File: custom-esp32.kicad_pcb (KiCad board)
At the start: 2 copper layers, 26 parts, among them J3 USB_C_Receptacle_USB2.0_16P, U1 ESD7104MUTAG, U2 ENS210, U3 ESP32-S3-MINI-1-N8, U4 TLV75801PDRV

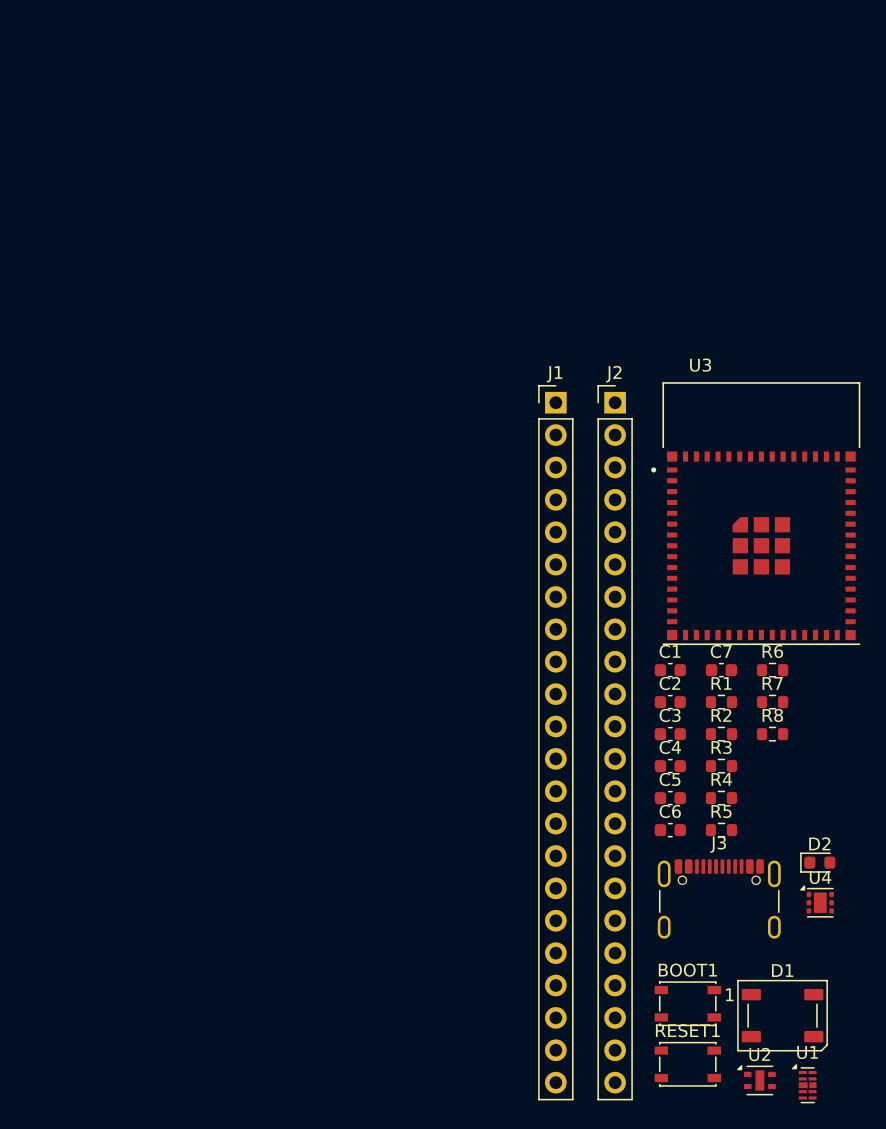
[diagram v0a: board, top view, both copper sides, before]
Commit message: Add initial pcb layout
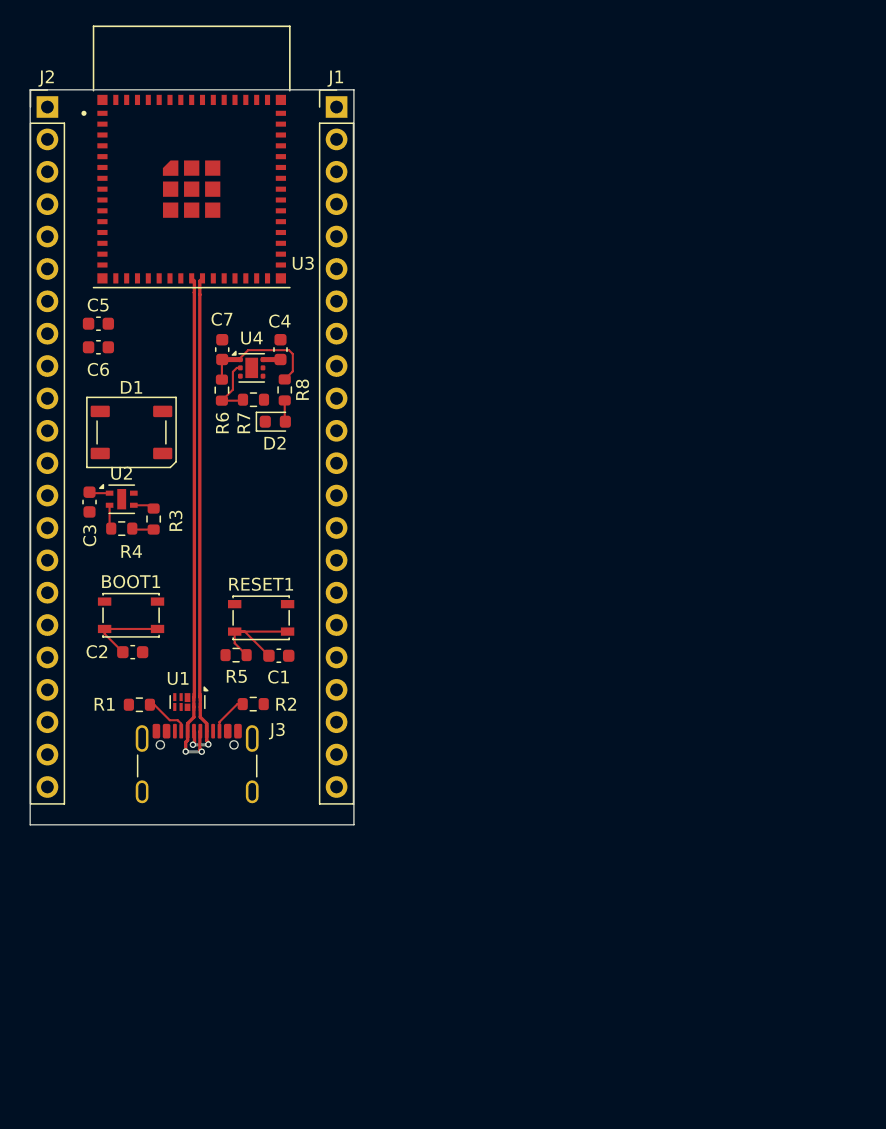
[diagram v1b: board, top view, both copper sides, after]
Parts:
- moved D1 68.6 mm to (97.5, 57.0)
- moved U2 67.7 mm to (96.7, 62.2)
- moved U4 61.2 mm to (106.9, 51.9)
- moved C6 58.7 mm to (94.9, 50.3)
- moved C5 58.3 mm to (94.9, 48.4)
- moved U1 57.2 mm to (101.9, 78.1), turned to -90 degrees
- moved D2 55.0 mm to (108.8, 56.1)
- moved BOOT1 53.3 mm to (97.5, 71.3)
- moved U3 52.7 mm to (102.2, 37.9)
- moved R4 51.6 mm to (96.7, 64.5)
- moved J2 50.2 mm to (90.9, 31.4)
- moved C3 49.1 mm to (94.2, 62.4), turned to -90 degrees
- moved R3 48.6 mm to (99.2, 63.8), turned to -90 degrees
- moved R6 48.5 mm to (104.6, 53.7), turned to 90 degrees
- moved RESET1 48.4 mm to (107.7, 71.5)
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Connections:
- U1 pad 10: unconnected-(U1-NC-Pad10) -> D+
- U1 pad 7: unconnected-(U1-NC-Pad7) -> 5VUSB
- U1 pad 9: unconnected-(U1-NC-Pad9) -> D-
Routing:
- net D-: track 0.00 -> 40.4 mm, vias 0 -> 2
- net D+: track 0.00 -> 39.3 mm, vias 0 -> 2
- net 3V3: track 0.00 -> 13.2 mm
- net ESP32_EN: track 0.00 -> 9.86 mm
- net GPIO0: track 0.00 -> 6.56 mm
- net Net-(U4-FB): track 0.00 -> 5.02 mm
- net Net-(J3-CC1): track 0.00 -> 3.66 mm
- net Net-(J3-CC2): track 0.00 -> 3.12 mm
- net I2C_SCL: track 0.00 -> 1.85 mm
- net Net-(D2-A): track 0.00 -> 1.69 mm
- net I2C_SDA: track 0.00 -> 1.66 mm
- net 5VUSB: track 0.00 -> 1.37 mm
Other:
- board outline added: 25.4 x 57.7 mm
- copper layers 2 -> 4

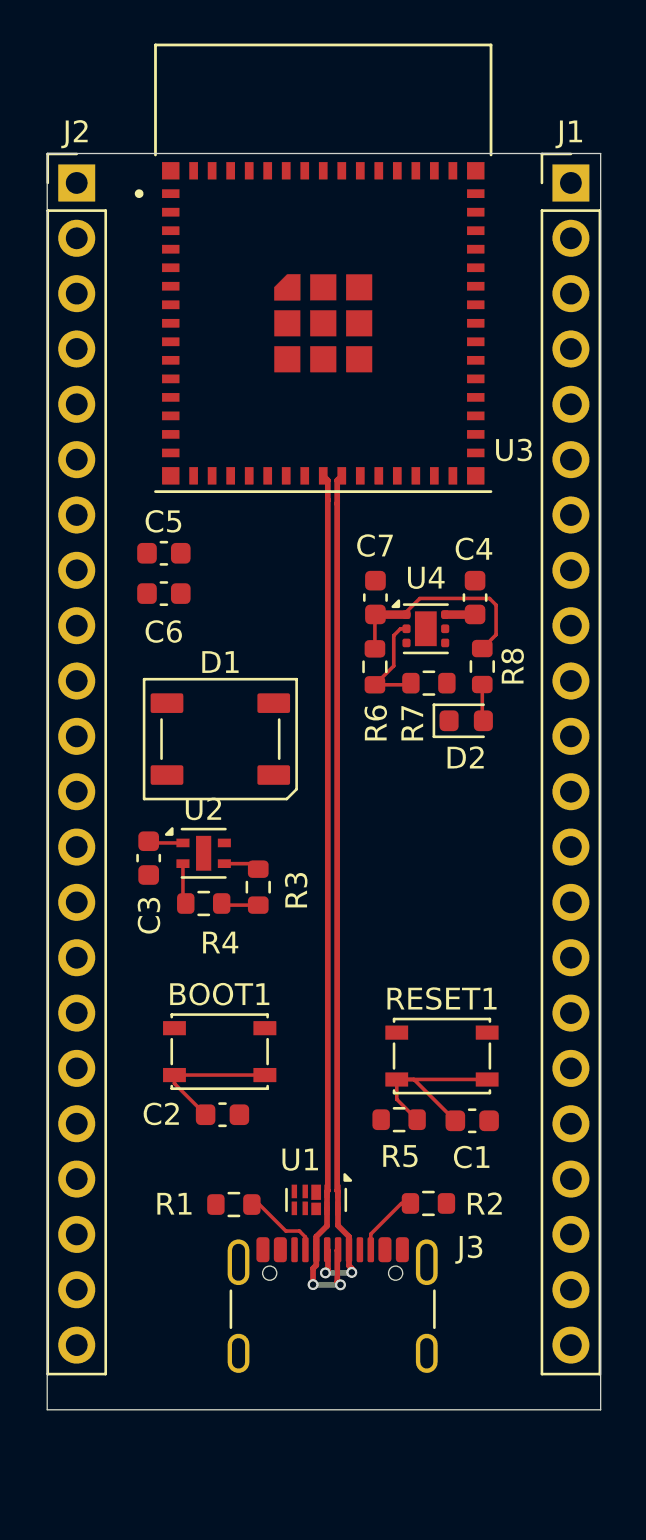
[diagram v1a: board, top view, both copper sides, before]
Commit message: Connect remaining components in pcb layout
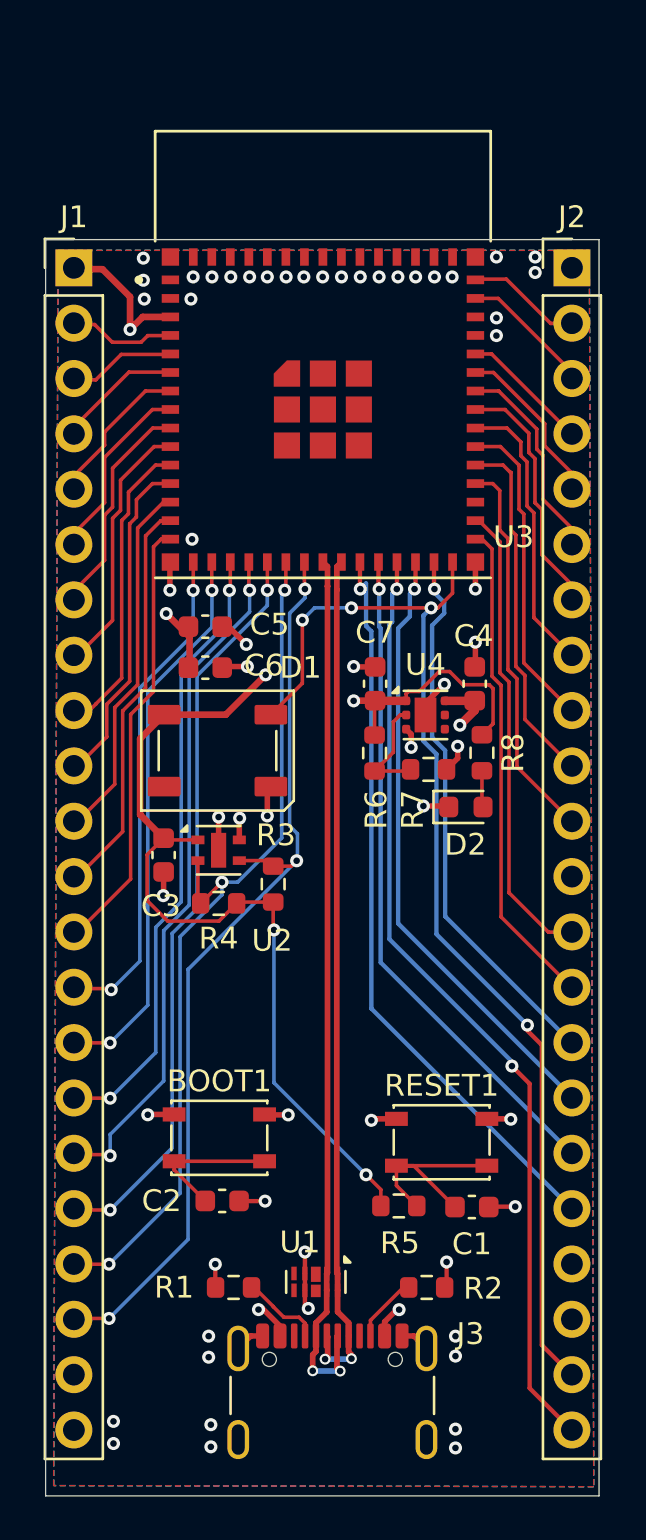
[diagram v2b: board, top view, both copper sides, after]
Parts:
- moved J1 23.1 mm to (90.8, 35.3)
- moved J2 23.1 mm to (113.6, 35.3)
- moved BOOT1 3.96 mm to (97.5, 75.3)
- moved C1 3.96 mm to (109.0, 78.4)
- moved C2 3.96 mm to (97.6, 78.2)
- moved R5 3.96 mm to (105.7, 78.4)
- moved RESET1 3.96 mm to (107.7, 75.5)
- moved C4 3.96 mm to (109.2, 54.4)
- moved C7 3.96 mm to (104.6, 54.4)
- moved D2 3.96 mm to (108.8, 60.1)
- moved R6 3.96 mm to (104.6, 57.6)
- moved R7 3.96 mm to (107.1, 58.4)
- moved R8 3.96 mm to (109.5, 57.6)
- moved U3 3.96 mm to (102.2, 41.8)
- moved U4 3.96 mm to (106.9, 55.9)
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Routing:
- net 3V3: track 13.2 -> 85.6 mm, vias 0 -> 6
- net GPIO48: track 0.00 -> 52.0 mm, vias 0 -> 4
- net 5VUSB: track 1.37 -> 52.0 mm, vias 0 -> 5
- net GPIO47: track 0.00 -> 43.5 mm, vias 0 -> 2
- net I2C_SDA: track 1.66 -> 43.1 mm, vias 0 -> 3
- net I2C_SCL: track 1.85 -> 40.8 mm, vias 0 -> 3
- net GPIO16: track 0.00 -> 34.3 mm, vias 0 -> 2
- net GPIO21: track 0.00 -> 34.2 mm, vias 0 -> 1
- net GPIO15: track 0.00 -> 31.5 mm, vias 0 -> 2
- net GPIO26: track 0.00 -> 30.8 mm, vias 0 -> 1
- net GND: track 0.00 -> 30.2 mm, vias 0 -> 57
- net GPIO14: track 0.00 -> 28.5 mm, vias 0 -> 2
- net GPIO33: track 0.00 -> 28.2 mm, vias 0 -> 1
- net GPIO13: track 0.00 -> 25.6 mm, vias 0 -> 2
- net GPIO34: track 0.00 -> 25.1 mm, vias 0 -> 1
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- added copper zone on B.Cu, net GND
- added copper zone on F.Cu, net GND
- added copper zone on In1.Cu, net GND
- added copper zone on In2.Cu, net GND

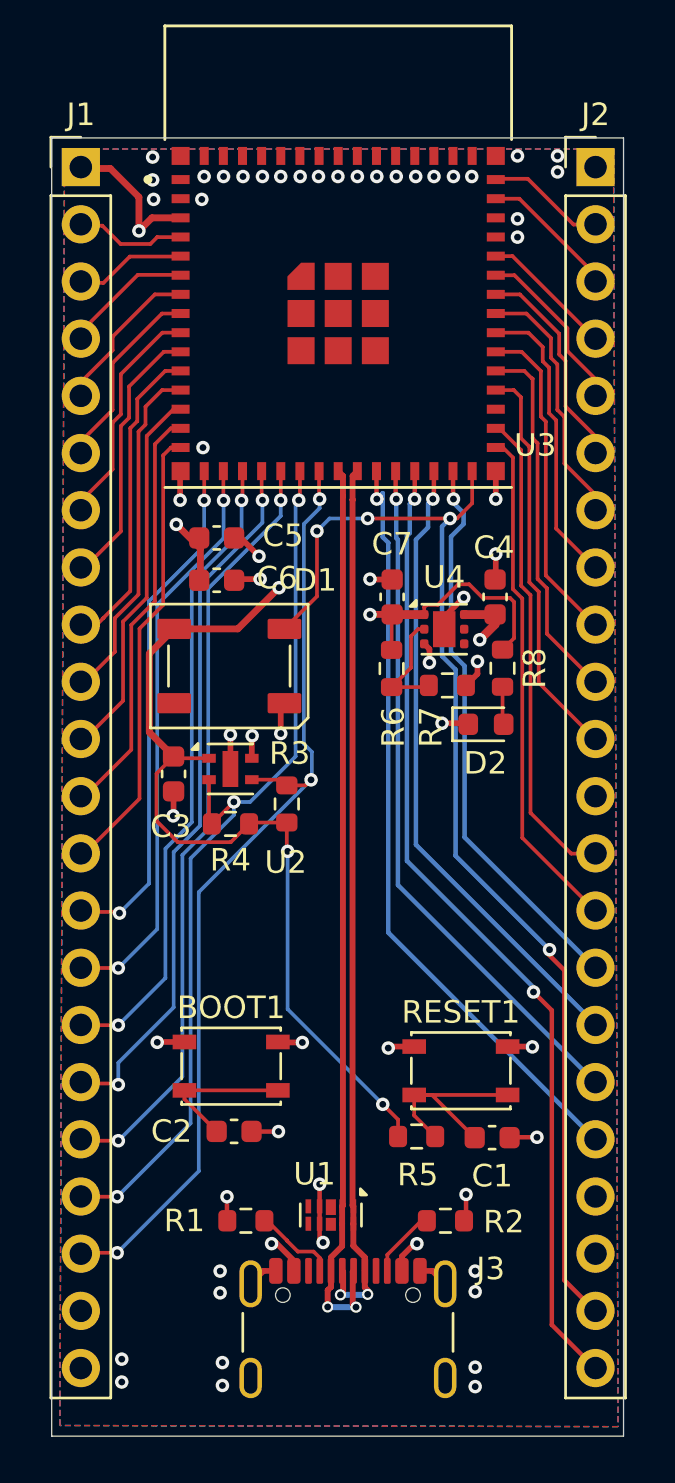
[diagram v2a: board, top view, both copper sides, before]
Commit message: Add missing 3d models and resolve design issues
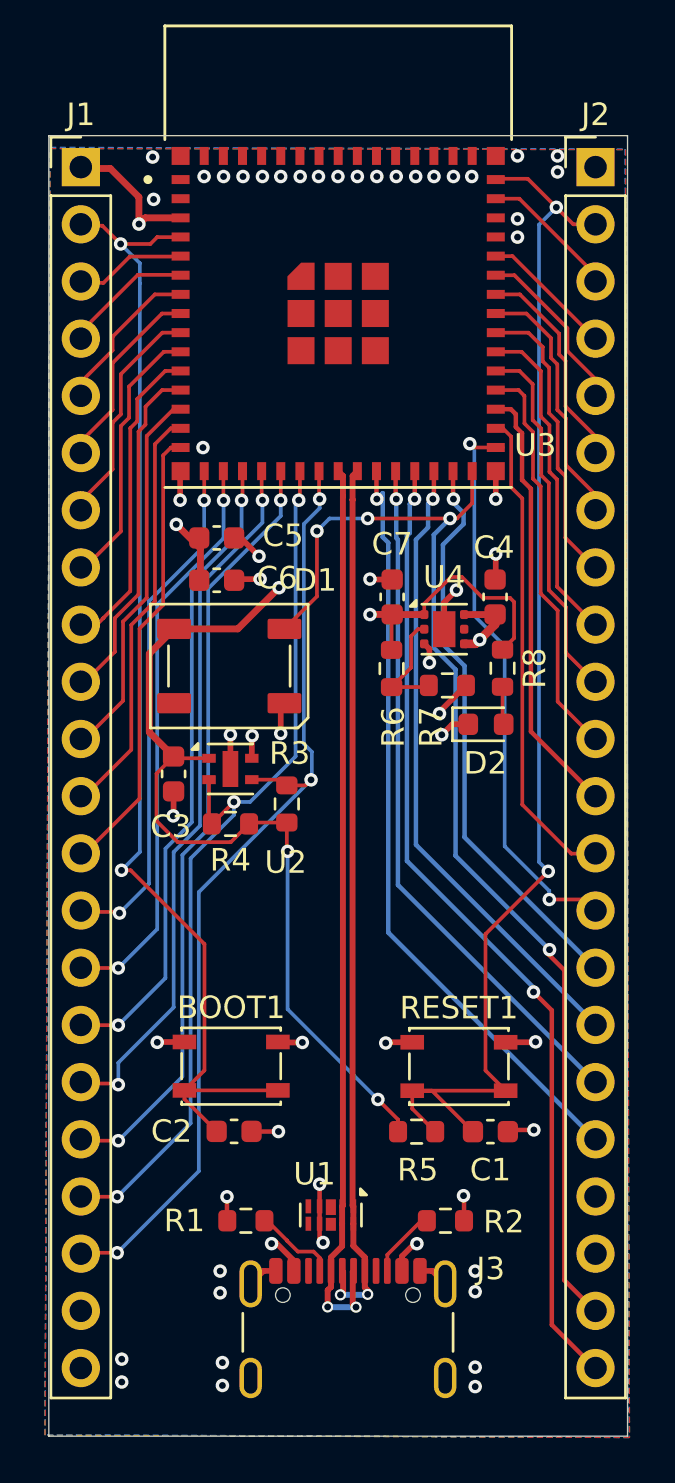
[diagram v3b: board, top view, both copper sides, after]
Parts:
- moved C1 0.28 mm to (109.0, 78.2)
- moved R5 0.22 mm to (105.7, 78.2)
- moved RESET1 0.21 mm to (107.6, 75.3)
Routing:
- net ESP32_EN: track 15.1 -> 56.4 mm, vias 0 -> 2
- net GPIO0: track 11.3 -> 51.8 mm, vias 0 -> 2
- net GPIO37: track 0.00 -> 19.4 mm
- net GPIO35: track 22.6 -> 25.5 mm, vias 0 -> 2
- net GND: track 30.2 -> 31.2 mm, vias 57 -> 55
- net 5VUSB: track 52.0 -> 52.8 mm
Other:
- board size 25.4 x 57.7 mm -> 25.7 x 57.8 mm

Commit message: Add fabrication files
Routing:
- net 3V3: track 85.6 -> 86.3 mm
- net GPIO21: track 34.2 -> 33.7 mm
- net GND: track 31.2 -> 31.4 mm, vias 55 -> 79
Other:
- board text added: "ImSeanConroy/Custom-ESP32 (v0.1)"
